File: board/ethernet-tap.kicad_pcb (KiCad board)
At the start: 4 copper layers, 139 x 92 mm, 417 parts, among them J1 BARREL_JACK, J10 XILINX_JTAG, J11 UART, J2 BEL_FUSE_0826-1G1T-23-F, J3 JUMPER_0402_SPDT, J4 JUMPER_0402_SPDT, J5 RJ45, J6 BEL_FUSE_0826-1G1T-23-F, J7 BEL_FUSE_0826-1G1T-23-F, J8 BEL_FUSE_0826-1G1T-23-F, J9 XILINX_JTAG, SW1 SWITCH, SW10 SWITCH, SW2 SWITCH, SW3 SWITCH, SW4 SWITCH, SW5 SWITCH, SW6 SWITCH, SW7 BUTTON, SW8 SWITCH, SW9 SWITCH, U1 LTC3374-QFN, U10 ECS-2016MVQ-250-CN-TR, U11 ECS-2016MVQ-250-CN-TR, U12 ECS-2016MVQ-250-CN-TR, U13 STM32H735-UFBGA176-25, U14 S25FLxxxS_BGA24_5x5_VIO, U2 KSZ9031RN, U3 MAX232, U4 XC7S15-1FTGB196C, U5 KSZ9031RN, U6 KSZ9031RN, U7 ECS-2016MVQ-250-CN-TR, U8 ECS-2016MVQ-250-CN-TR, U9 KSZ9031RN

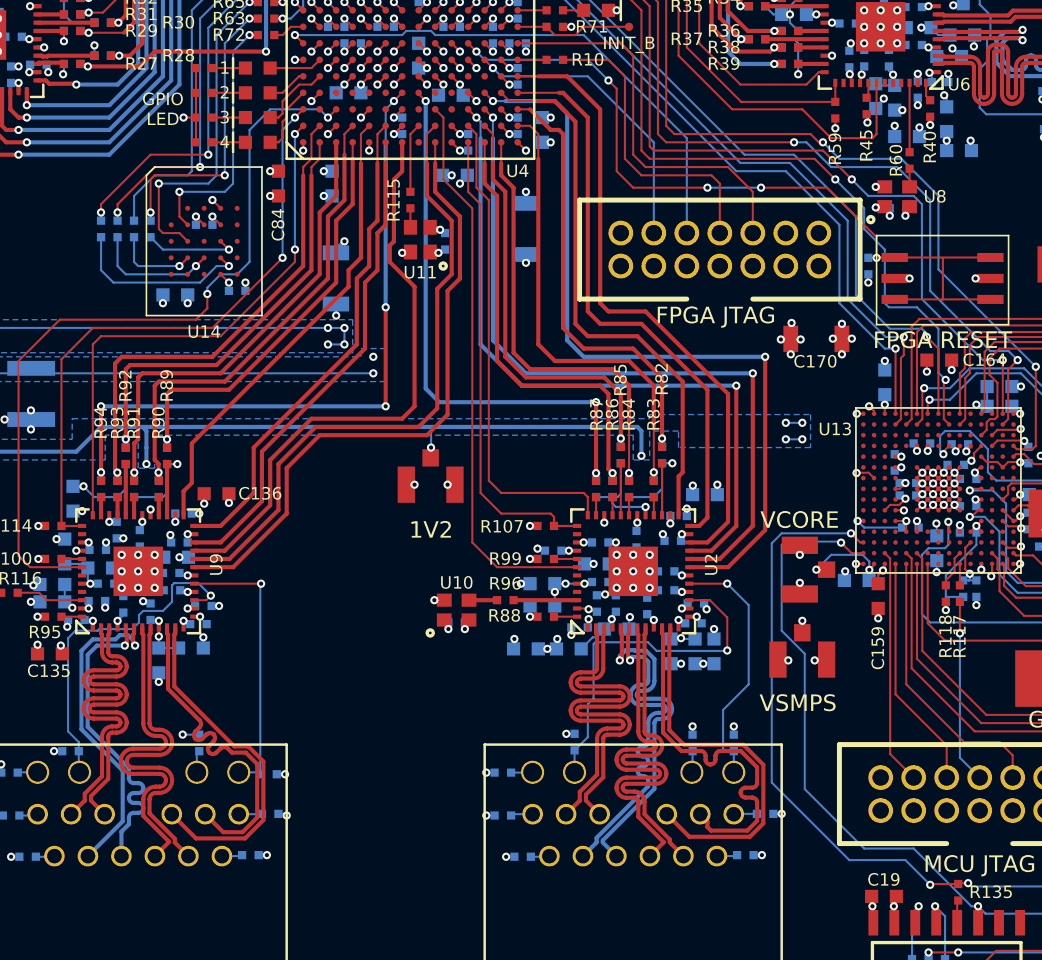
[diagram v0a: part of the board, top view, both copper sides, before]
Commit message: Finished power plane routing, moved some signals around to reduce layer split crossings
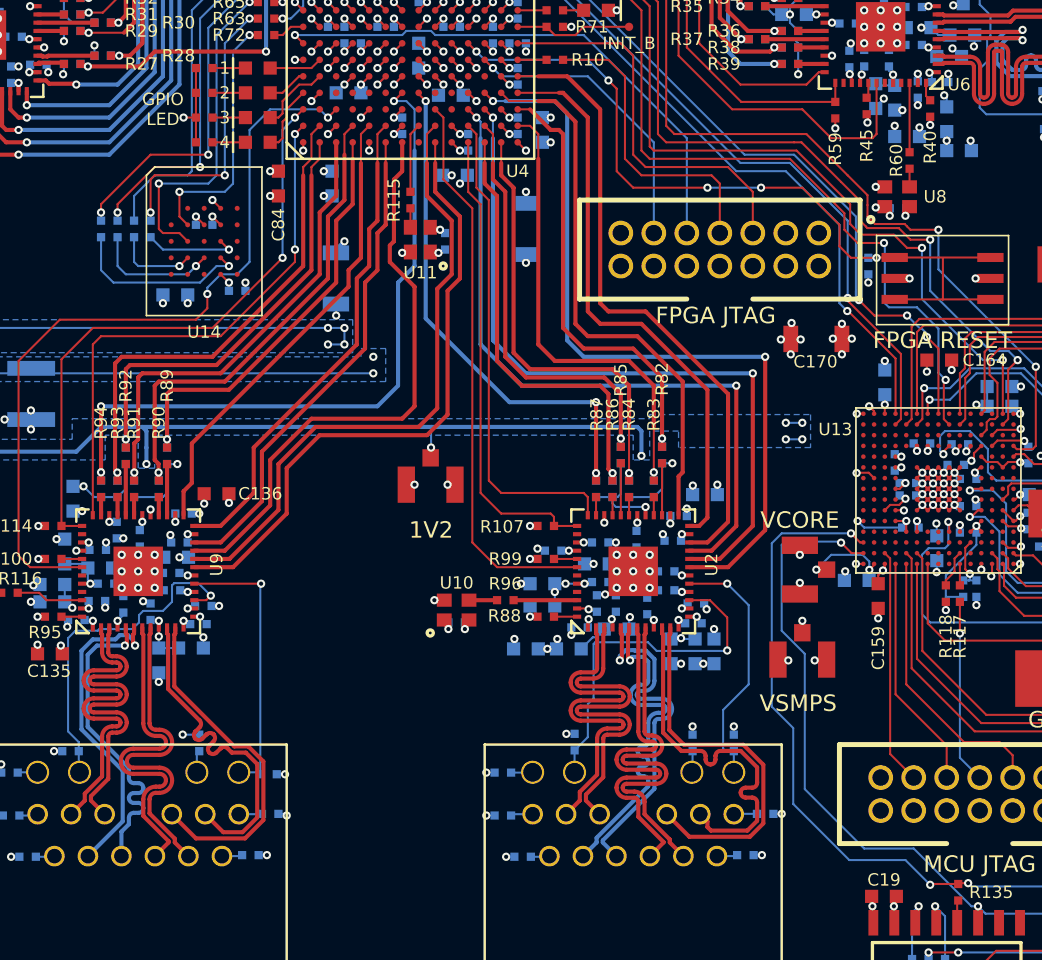
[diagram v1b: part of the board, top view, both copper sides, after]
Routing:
- net /GND: track 1487.1 -> 1520.8 mm
- net /3V3: track 823.9 -> 818.0 mm
- net /Management Interface/VSMPS: track 58.7 -> 62.5 mm
- net /Monitor Path/ETH2_RGMII_RX_CLK: track 33.9 -> 31.4 mm
- net /Monitor Path/ETH2_A3V3: track 13.1 -> 11.2 mm
- net /Monitor Path/ETH3_RGMII_RX_CLK: track 41.7 -> 42.8 mm, vias 5 -> 3
- net /Management Interface/FPGA_SPI_DQ0: track 51.6 -> 50.8 mm
- net /Management Interface/FPGA_SPI_DQ3: track 52.1 -> 51.4 mm
- net /Management Interface/FPGA_IRQ: track 45.1 -> 44.5 mm
- net /1V0: track 132.7 -> 133.3 mm
- net /Management Interface/FPGA_SPI_DQ1: track 47.5 -> 47.8 mm, vias 2 -> 4
- added copper zone on In1.Cu, net /GND
- added copper zone on In2.Cu, net /Management Interface/VCORE
- added copper zone on In2.Cu, net /Management Interface/VSMPS
- added copper zone on In2.Cu, net /Monitor Path/ETH2_A1V2
- added copper zone on In2.Cu, net /Monitor Path/ETH2_A1V2_PLL
- added copper zone on In2.Cu, net /Monitor Path/ETH2_A3V3
- added copper zone on In2.Cu, net /Thru Path/ETH1_A1V2
- added copper zone on In2.Cu, net /Thru Path/ETH1_A3V3

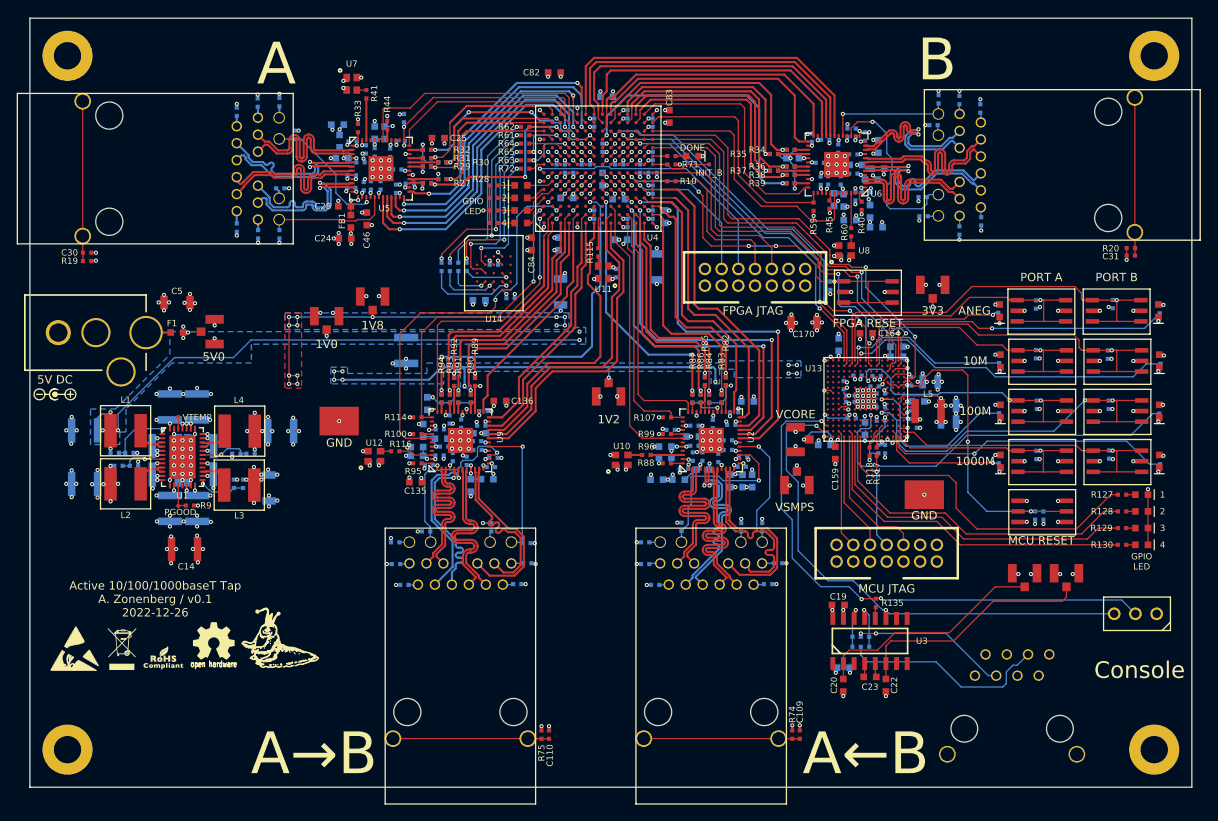
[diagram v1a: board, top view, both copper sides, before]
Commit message: DRC fixes to layout
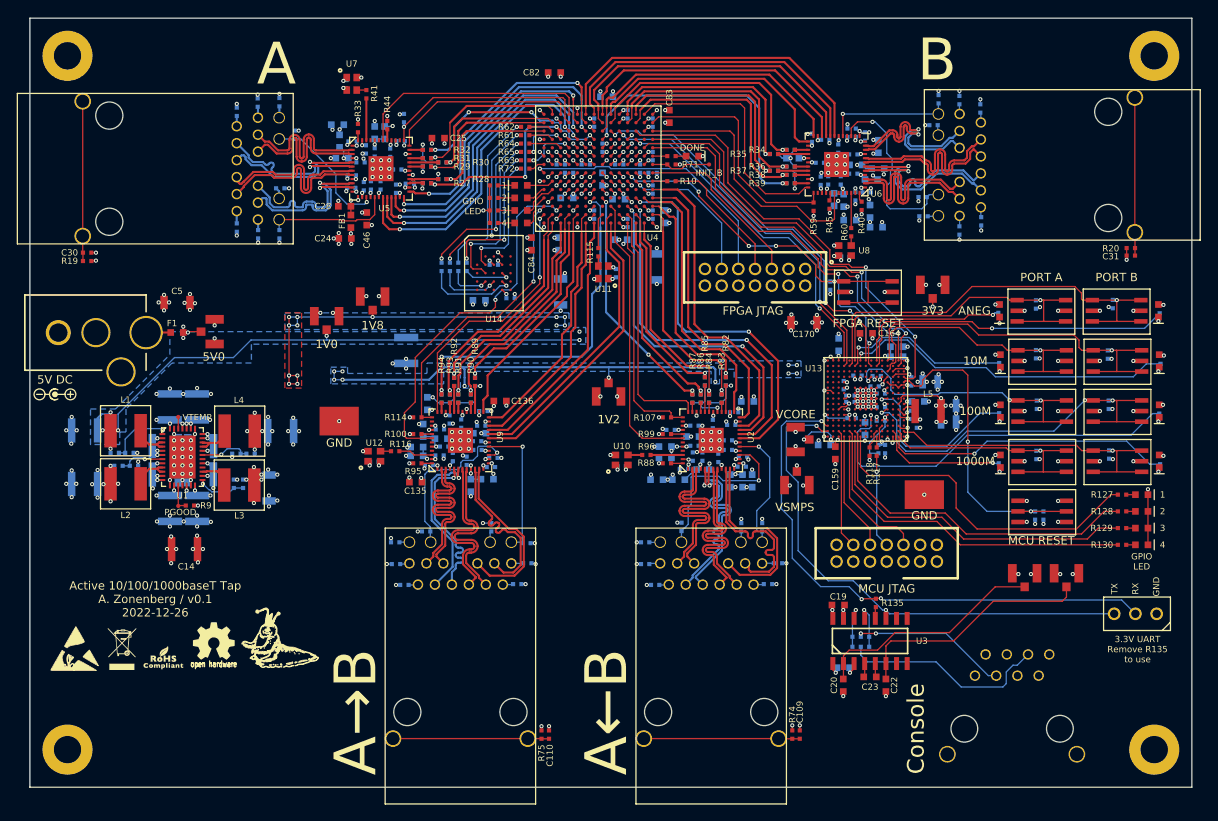
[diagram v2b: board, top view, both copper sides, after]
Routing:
- net /GND: track 1520.8 -> 1506.6 mm
- net /Monitor Path/ETH3_RGMII_TXD2: track 35.5 -> 31.3 mm
- net /Monitor Path/ETH3_RGMII_TXD1: track 38.4 -> 35.2 mm
- net /Monitor Path/ETH3_RGMII_TXD0: track 38.2 -> 34.9 mm
- net /Monitor Path/ETH3_RST_N: track 47.3 -> 44.1 mm
- net /FPGA Support/FPGA_JTAG_TDI: track 24.0 -> 21.1 mm
- net /Management Interface/FPGA_SPI_DQ0: track 50.8 -> 48.0 mm
- net /Management Interface/FPGA_SPI_SCK: track 47.7 -> 45.0 mm
- net /FPGA Support/FPGA_RST_N: track 49.0 -> 46.4 mm
- net /Monitor Path/ETH2_RGMII_RX_CLK: track 31.4 -> 28.9 mm
- net /FPGA Support/FPGA_JTAG_TDO: track 18.5 -> 16.0 mm
- net /Management Interface/FPGA_SPI_DQ3: track 51.4 -> 49.0 mm
- net /Monitor Path/ETH2_RGMII_RX_DV: track 26.9 -> 24.7 mm
- net /Management Interface/FPGA_SPI_DQ2: track 56.8 -> 54.5 mm
- net /Thru Path/ETH1_RGMII_TXD2: track 40.5 -> 38.4 mm
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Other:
- board text added: "3.3V UART Remove R135 to use"
- board text added: "RX"
- board text added: "TX"

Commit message: Final v0.1 layout after design review
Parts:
- added C185: 0.47 uF, azonenberg_pcb:EIA_0402_CAP_NOSILK, B.Cu at (94.1, 61.8)
- added C186: 0.47 uF, azonenberg_pcb:EIA_0402_CAP_NOSILK, B.Cu at (107.9, 59.5)
- added C187: 0.47 uF, azonenberg_pcb:EIA_0402_CAP_NOSILK, F.Cu at (71.1, 32.0)
- added J12: SMA, azonenberg_pcb:CONN_SMA_EDGE_SAMTEC_SMA_J_P_H_ST_EM1, B.Cu at (77.3, 21.0)
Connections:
- U4 pad L12: unconnected-(U4-PadL12) -> /Thru Path/TRIG_OUT
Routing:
- net /GND: track 1506.6 -> 1549.1 mm, vias 377 -> 390
- net /Thru Path/TRIG_OUT: track 0.00 -> 41.2 mm, vias 0 -> 3
- net /3V3: track 817.8 -> 828.2 mm, vias 127 -> 130
- net /Thru Path/ETH1_RGMII_RX_CLK: track 35.1 -> 29.4 mm
- net /Thru Path/ETH1_RGMII_TXD0: track 40.8 -> 44.2 mm
- net /Thru Path/ETH1_RGMII_TXD2: track 38.4 -> 41.4 mm
- net /Thru Path/ETH1_RGMII_TXD1: track 39.0 -> 42.1 mm
- net /Monitor Path/ETH2_RGMII_TXD1: track 43.0 -> 40.2 mm
- net /Thru Path/ETH1_RGMII_TXD3: track 34.6 -> 37.3 mm
- net /Monitor Path/ETH2_RGMII_TXD2: track 41.6 -> 39.0 mm
- net /Monitor Path/ETH2_RGMII_TXD0: track 45.7 -> 43.1 mm
- net /Thru Path/ETH1_RGMII_TX_CLK: track 34.2 -> 36.7 mm
- net /Thru Path/ETH1_RGMII_TX_EN: track 31.2 -> 32.6 mm
- net /Boot Flash/FLASH_DQ1: track 20.8 -> 19.6 mm
- net /Thru Path/ETH1_LED2_N: track 22.7 -> 21.7 mm
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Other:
- board text added: "Active 10/100/1000baseT Tap A. Zonenberg / v0.1 2022-12-27"
- board text added: "TRIG OUT 3.3V CMOS"
- board text removed: "Active 10/100/1000baseT Tap A. Zonenberg / v0.1 2022-12-26"
